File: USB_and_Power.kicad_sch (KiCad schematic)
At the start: 20 parts, among them J1 USB_C_Receptacle_USB2.0_14P, U3 BQ24074RGT, U4 FUSB303BTMX

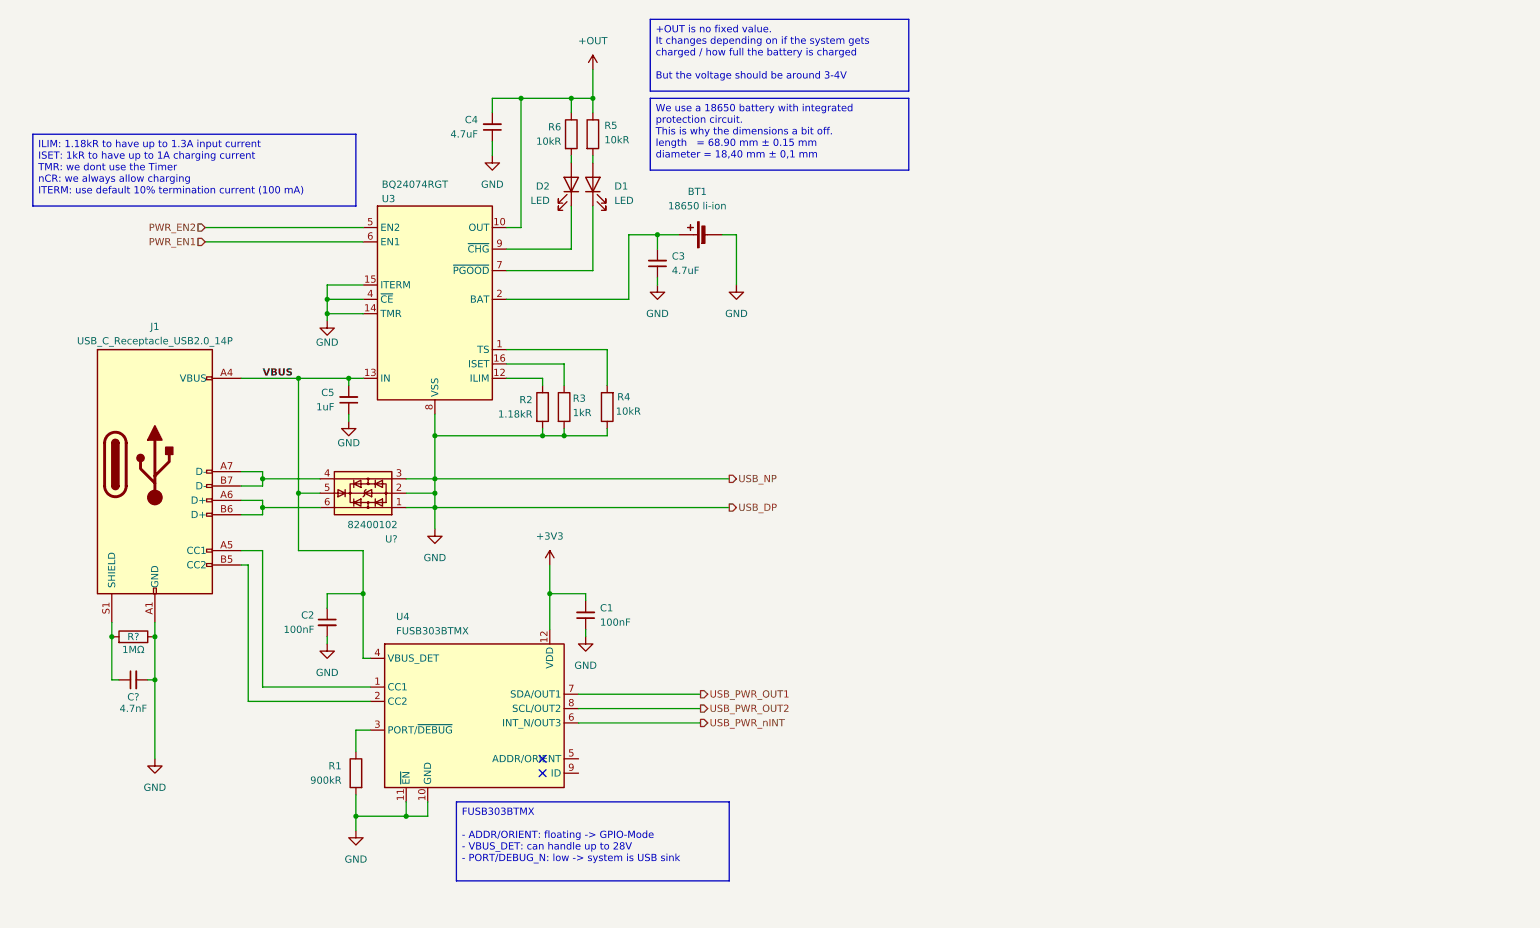
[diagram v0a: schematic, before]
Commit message: Added 5V, 3V3, PAM circuit
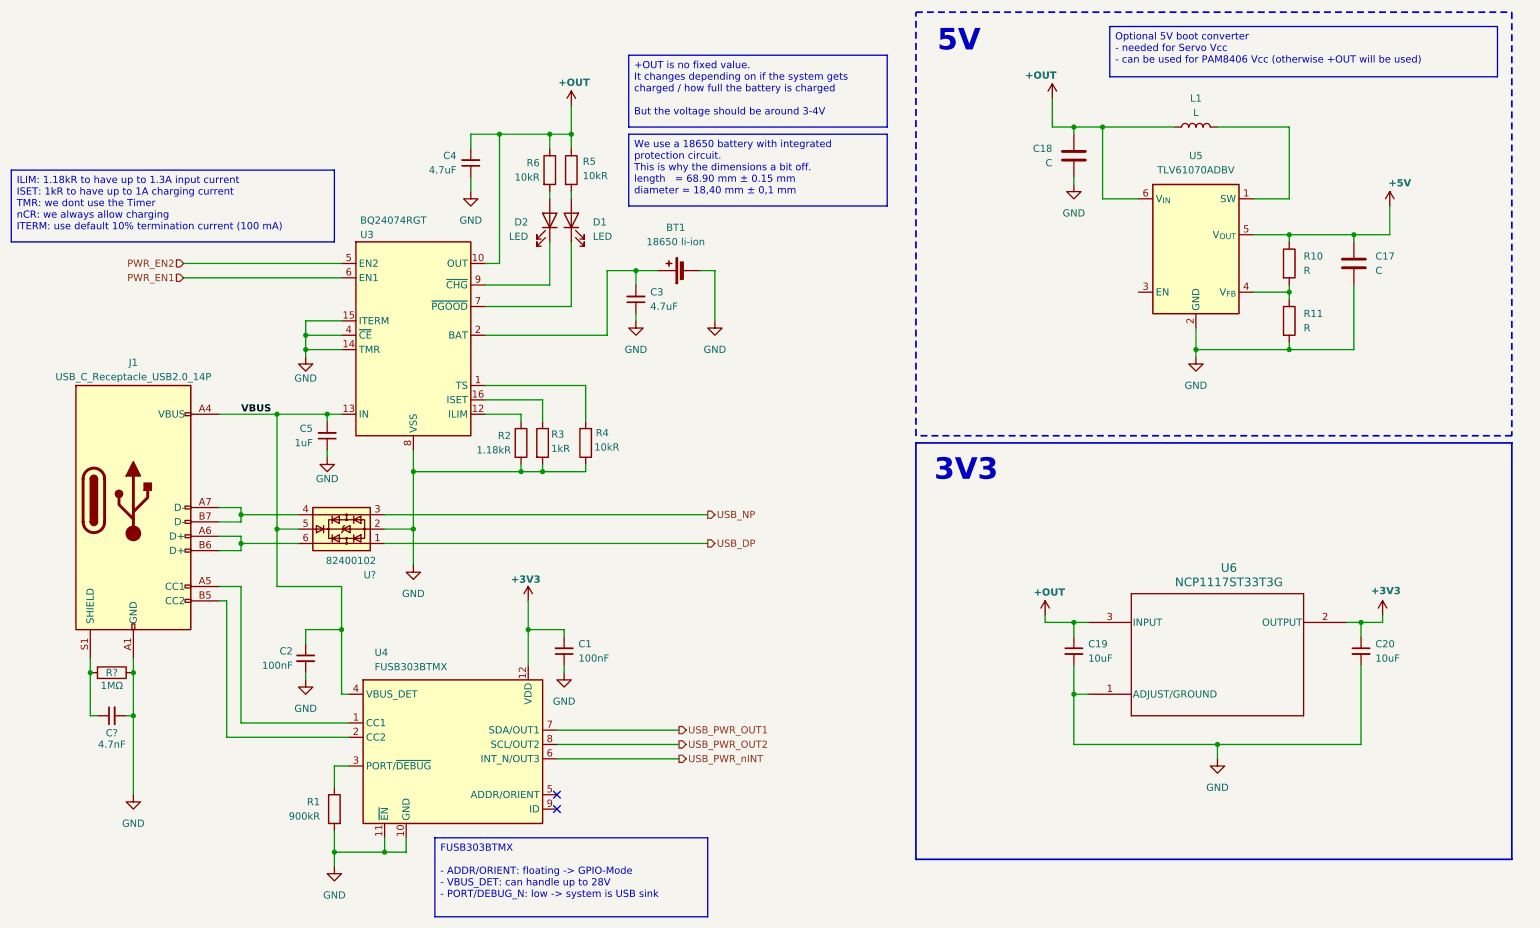
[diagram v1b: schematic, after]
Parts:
- added C17, C18: C, symbol Device:C
- added C19, C20: 10uF, Capacitor_SMD:C_0805_2012Metric_Pad1.18x1.45mm_HandSolder, symbol Device:C_Small
- added L1: L, symbol Device:L
- added R10, R11: R, symbol Device:R
- added U5: TLV61070ADBV, Package_DFN_QFN:Texas_RWU0007A_VQFN-7_2x2mm_P0.5mm, symbol Regulator_Switching:TLV61070ADBV
- added U6: NCP1117ST33T3G, NCP1117ST33T3G:SOT223-3_ONS, symbol NCP1117ST33T3G:NCP1117ST33T3G
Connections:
- net +3V3: now also C20.1, U6.2 (OUTPUT)
- net +OUT: now also C18.1, C19.1, L1.1, U5.6 (V_{IN}), U6.3 (INPUT)
- net GND: now also C17.2, C18.2, C19.2, C20.2, R11.2, U5.2 (GND), U6.1 (ADJUST/GROUND); no longer U?.1, U?.3
- new net: L1.2, U5.1 (SW)
- new net: R10.2, R11.1, U5.4 (V_{FB})
- new net +5V: C17.1, R10.1, U5.5 (V_{OUT})
- new net USB_DP: U?.1
- new net USB_NP: U?.3
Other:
- note added: "3V3"
- note added: "5V"
- company: (none) -> Author: Christian R
- title: (none) -> Snail v1
- moved on the sheet: BT1, C1, C2, C3, C4, C5, C?, D1, D2, J1, R1, R2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

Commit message: Added BY25Q32 extFlash
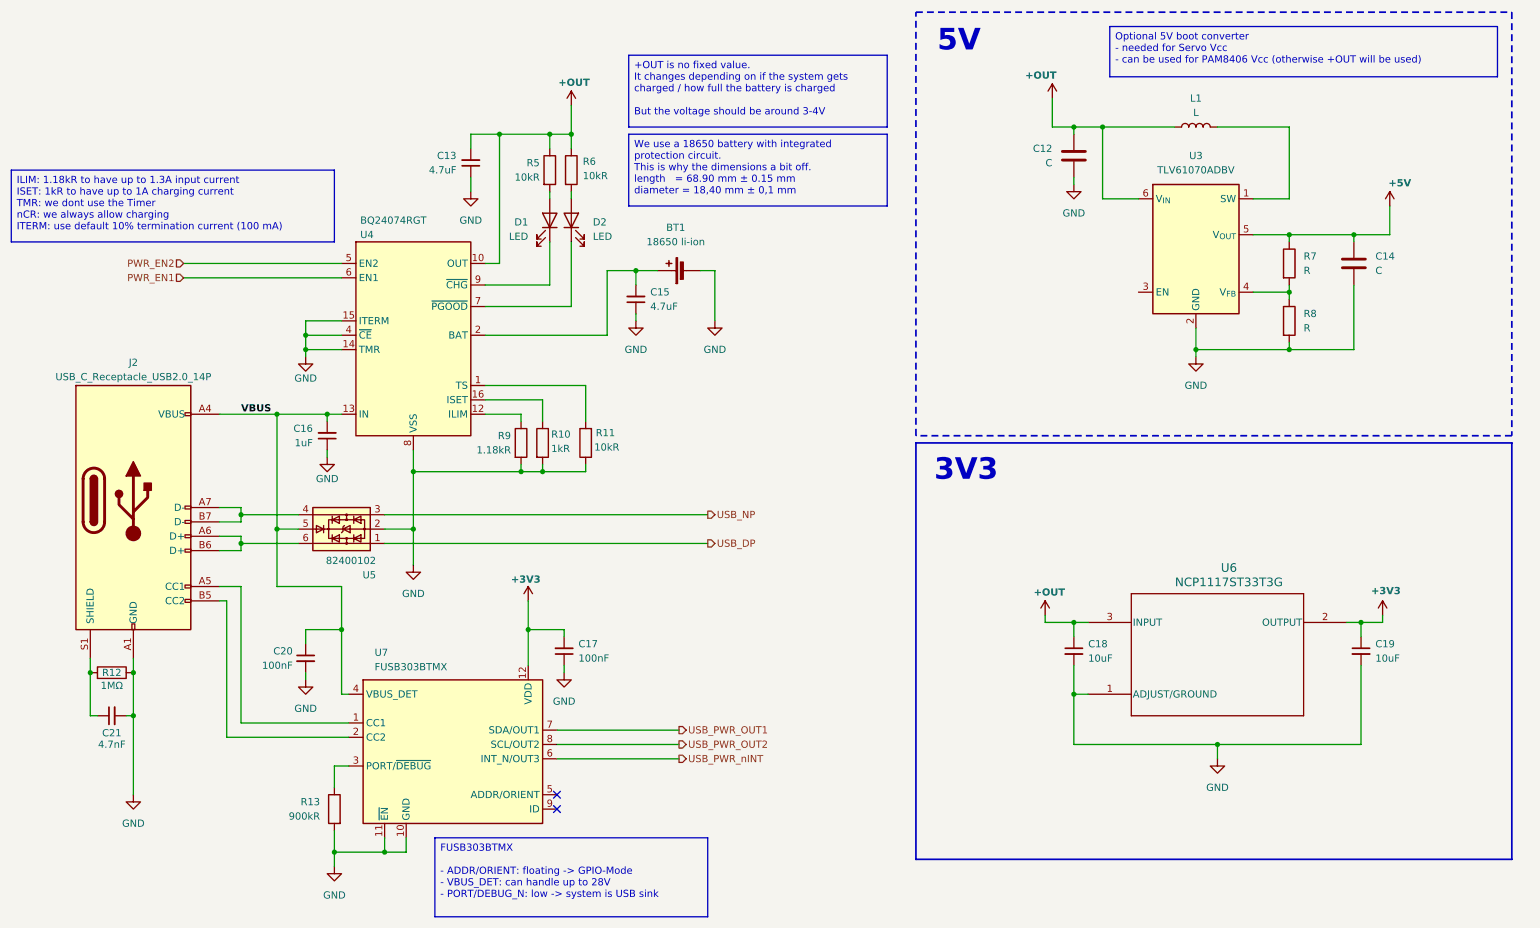
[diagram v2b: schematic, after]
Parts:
- gave numbers to parts that had none: 3
- renumbered C18 to C12, C4 to C13, C17 to C14, C3 to C15, C5 to C16, C1 to C17, C19 to C18, C20 to C19, C2 to C20, D2 to D1, D1 to D2, J1 to J2, R3 to R10, R4 to R11, R1 to R13, R6 to R5, R5 to R6, R10 to R7, R11 to R8, R2 to R9, U5 to U3, U3 to U4, U4 to U7

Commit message: Changed LDO to Buc-Boost
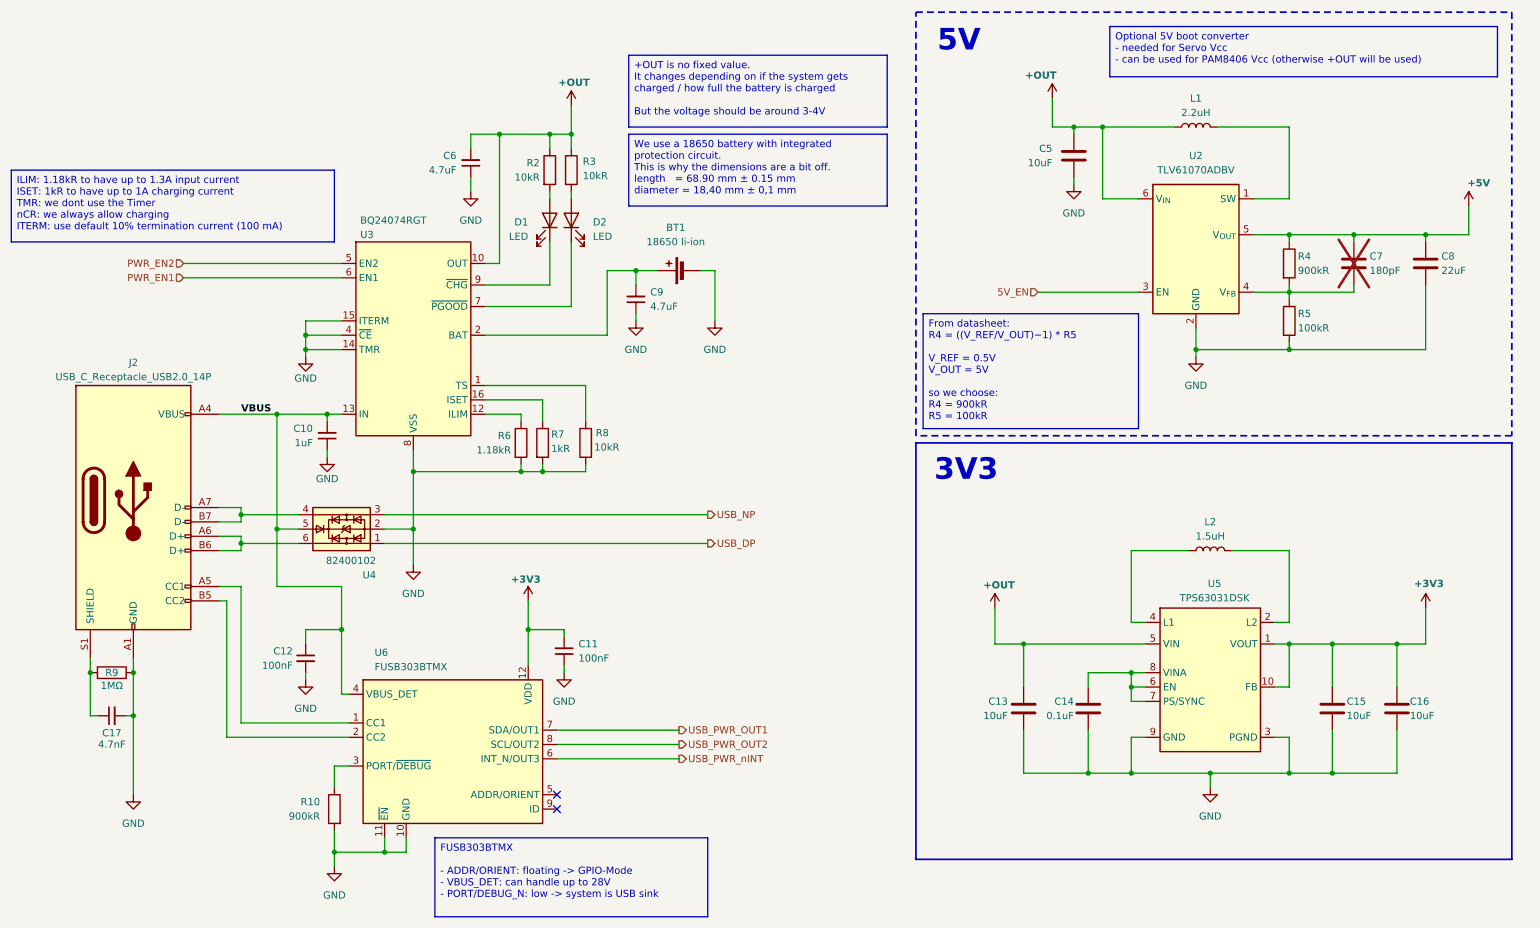
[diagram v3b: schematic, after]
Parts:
- removed C18, C19: 10uF, Capacitor_SMD:C_0805_2012Metric_Pad1.18x1.45mm_HandSolder, symbol Device:C_Small
- removed U6: NCP1117ST33T3G, NCP1117ST33T3G:SOT223-3_ONS, symbol NCP1117ST33T3G:NCP1117ST33T3G
- added C13, C15, C16: 10uF, Capacitor_SMD:C_0805_2012Metric_Pad1.18x1.45mm_HandSolder, symbol Device:C
- added C14: 0.1uF, Capacitor_SMD:C_0805_2012Metric_Pad1.18x1.45mm_HandSolder, symbol Device:C
- added C8: 22uF, Capacitor_SMD:C_0805_2012Metric_Pad1.18x1.45mm_HandSolder, symbol Device:C
- added L2: 1.5uH, Inductor_SMD:L_0805_2012Metric_Pad1.05x1.20mm_HandSolder, symbol Device:L
- added U5: TPS63031DSK, Package_SON:WSON-10-1EP_2.5x2.5mm_P0.5mm_EP1.2x2mm, symbol Regulator_Switching:TPS63031DSK
- C10: renamed from C16; footprint (none) -> Capacitor_SMD:C_0805_2012Metric_Pad1.18x1.45mm_HandSolder
- C11: renamed from C17; footprint (none) -> Capacitor_SMD:C_0805_2012Metric_Pad1.18x1.45mm_HandSolder
- C12: renamed from C20; footprint (none) -> Capacitor_SMD:C_0805_2012Metric_Pad1.18x1.45mm_HandSolder
- C5: renamed from C12; value C -> 10uF; footprint (none) -> Capacitor_SMD:C_0805_2012Metric_Pad1.18x1.45mm_HandSolder
- C6: renamed from C13; footprint (none) -> Capacitor_SMD:C_0805_2012Metric_Pad1.18x1.45mm_HandSolder
- C7: renamed from C14; value C -> 180pF; footprint (none) -> Capacitor_SMD:C_0805_2012Metric_Pad1.18x1.45mm_HandSolder; now not fitted
- C9: renamed from C15; footprint (none) -> Capacitor_SMD:C_0805_2012Metric_Pad1.18x1.45mm_HandSolder
- D1, D2: footprint (none) -> LED_SMD:LED_0805_2012Metric_Pad1.15x1.40mm_HandSolder
- J2: footprint (none) -> Connector_USB:USB_C_Receptacle_GCT_USB4105-xx-A_16P_TopMnt_Horizontal
- L1: value L -> 2.2uH; footprint (none) -> Inductor_SMD:L_0805_2012Metric_Pad1.05x1.20mm_HandSolder
- R10: renamed from R13; footprint (none) -> Resistor_SMD:R_0805_2012Metric_Pad1.20x1.40mm_HandSolder
- R2: renamed from R5; footprint (none) -> Resistor_SMD:R_0805_2012Metric_Pad1.20x1.40mm_HandSolder
- R3: renamed from R6; footprint (none) -> Resistor_SMD:R_0805_2012Metric_Pad1.20x1.40mm_HandSolder
- R4: renamed from R7; value R -> 900kR; footprint (none) -> Resistor_SMD:R_0805_2012Metric_Pad1.20x1.40mm_HandSolder
- R5: renamed from R8; value R -> 100kR; footprint (none) -> Resistor_SMD:R_0805_2012Metric_Pad1.20x1.40mm_HandSolder
- R6: renamed from R9; footprint (none) -> Resistor_SMD:R_0805_2012Metric_Pad1.20x1.40mm_HandSolder
- R7: renamed from R10; footprint (none) -> Resistor_SMD:R_0805_2012Metric_Pad1.20x1.40mm_HandSolder
- R8: renamed from R11; footprint (none) -> Resistor_SMD:R_0805_2012Metric_Pad1.20x1.40mm_HandSolder
- renumbered C21 to C17, R12 to R9, U3 to U2, U4 to U3, U5 to U4, U7 to U6
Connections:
- net +3V3: now also C15.1, C16.1, U5.1 (VOUT), U5.10 (FB)
- net +5V: now also C8.1
- net +OUT: now also C13.1, U5.5 (VIN)
- net GND: now also C13.2, C14.2, C15.2, C16.2, C8.2, U5.3 (PGND), U5.9 (GND); no longer C7.2
- net 5V_EN: now reaches U2.3 (EN)
- net at R4.2, R5.1, U2.4 (V_{FB}): now also C7.2
- new net: L2.2, U5.2 (L2)
- new net: L2.1, U5.4 (L1)
- new net: C14.1, U5.6 (EN), U5.7 (PS/SYNC), U5.8 (VINA)

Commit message: Added LEDs + TPs
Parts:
- BT1: footprint (none) -> Battery:BatteryHolder_MPD_BH-18650-PC
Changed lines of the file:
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@@
 			)
 		)
-		(property "Footprint" ""
+		(property "Footprint" "Battery:BatteryHolder_MPD_BH-18650-PC"
 			(at 135.636 59.69 90)
 			(effects

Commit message: Started with layout
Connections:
- net +OUT: now also D1.2 (A), D2.2 (A); no longer R2.1, R3.1
- net at D2.1 (K): now also R3.1; no longer U3.7 (~{PGOOD})
- net at R3.2: now also U3.7 (~{PGOOD}); no longer D2.2 (A)
- net at U3.9 (~{CHG}): now also R2.2; no longer D1.1 (K)
- net USB_DP renamed USB+
- net USB_NP renamed USB-
- new net: D1.1 (K), R2.1
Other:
- moved on the sheet: D1, D2, R2, R3
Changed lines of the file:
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@@
 		)
 	)
-	(hierarchical_label "USB_NP"
+	(hierarchical_label "USB-"
 		(shape output)
 		(at 140.97 102.87 0)
@@
 		)
 	)
-	(hierarchical_label "USB_DP"
+	(hierarchical_label "USB+"
 		(shape output)
 		(at 140.97 107.95 0)
@@
 	(symbol
 		(lib_id "Device:LED")
-		(at 116.84 50.8 90)
+		(at 116.84 41.91 90)
 		(unit 1)
 		(exclude_from_sim no)
@@
 		(fields_autoplaced yes)
 		(property "Reference" "D2"
-			(at 120.65 51.1174 90)
+			(at 120.65 42.2274 90)
 			(effects
 				(font
@@
 		)
 		(property "Value" "LED"
-			(at 120.65 53.6574 90)
+			(at 120.65 44.7674 90)
 			(effects
 				(font
@@
 		)
 		(property "Footprint" "LED_SMD:LED_0805_2012Metric_Pad1.15x1.40mm_HandSolder"
-			(at 116.84 50.8 0)
+			(at 116.84 41.91 0)
 			(effects
 				(font
@@
 		)
 		(property "Datasheet" "~"
-			(at 116.84 50.8 0)
+			(at 116.84 41.91 0)
 			(effects
 				(font
@@
 		)
 		(property "Description" "Light emitting diode"
-			(at 116.84 50.8 0)
+			(at 116.84 41.91 0)
 			(effects
 				(font
@@
 		)
 		(property "Sim.Pins" "1=K 2=A"
-			(at 116.84 50.8 0)
+			(at 116.84 41.91 0)
 			(effects
 				(font
@@
 	(symbol
 		(lib_id "Device:LED")
-		(at 113.03 50.8 270)
+		(at 113.03 41.91 270)
 		(mirror x)
 		(unit 1)
@@
 		(dnp no)
 		(property "Reference" "D1"
-			(at 109.22 51.1174 90)
+			(at 109.22 42.2274 90)
 			(effects
 				(font
@@
 		)
 		(property "Value" "LED"
-			(at 109.22 53.6574 90)
+			(at 109.22 44.7674 90)
 			(effects
 				(font
@@
 		)
 		(property "Footprint" "LED_SMD:LED_0805_2012Metric_Pad1.15x1.40mm_HandSolder"
-			(at 113.03 50.8 0)
+			(at 113.03 41.91 0)
 			(effects
 				(font
@@
 		)
 		(property "Datasheet" "~"
-			(at 113.03 50.8 0)
+			(at 113.03 41.91 0)
 			(effects
 				(font
@@
 		)
 		(property "Description" "Light emitting diode"
-			(at 113.03 50.8 0)
+			(at 113.03 41.91 0)
 			(effects
 				(font
@@
 		)
 		(property "Sim.Pins" "1=K 2=A"
-			(at 113.03 50.8 0)
+			(at 113.03 41.91 0)
 			(effects
 				(font
@@
 	(symbol
 		(lib_id "Device:R")
-		(at 116.84 41.91 0)
+		(at 116.84 50.8 0)
 		(unit 1)
 		(exclude_from_sim no)
@@
 		(dnp no)
 		(property "Reference" "R3"
-			(at 118.872 40.386 0)
+			(at 118.872 49.276 0)
 			(effects
 				(font
@@
 		)
 		(property "Value" "10kR"
-			(at 118.872 42.926 0)
+			(at 118.872 51.816 0)
 			(effects
 				(font
@@
 		)
 		(property "Footprint" "Resistor_SMD:R_0805_2012Metric_Pad1.20x1.40mm_HandSolder"
-			(at 115.062 41.91 90)
+			(at 115.062 50.8 90)
 			(effects
 				(font
@@
 		)
 		(property "Datasheet" "~"
-			(at 116.84 41.91 0)
+			(at 116.84 50.8 0)
 			(effects
 				(font
@@
 		)
 		(property "Description" "Resistor"
-			(at 116.84 41.91 0)
+			(at 116.84 50.8 0)
 			(effects
 				(font
@@
 	(symbol
 		(lib_id "Device:R")
-		(at 113.03 41.91 0)
+		(at 113.03 50.8 0)
 		(unit 1)
 		(exclude_from_sim no)
@@
 		(dnp no)
 		(property "Reference" "R2"
-			(at 111.252 40.64 0)
+			(at 111.252 49.53 0)
 			(effects
 				(font
@@
 		)
 		(property "Value" "10kR"
-			(at 111.252 43.18 0)
+			(at 111.252 52.07 0)
 			(effects
 				(font
@@
 		)
 		(property "Footprint" "Resistor_SMD:R_0805_2012Metric_Pad1.20x1.40mm_HandSolder"
-			(at 111.252 41.91 90)
+			(at 111.252 50.8 90)
 			(effects
 				(font
@@
 		)
 		(property "Datasheet" "~"
-			(at 113.03 41.91 0)
+			(at 113.03 50.8 0)
 			(effects
 				(font
@@
 		)
 		(property "Description" "Resistor"
-			(at 113.03 41.91 0)
+			(at 113.03 50.8 0)
 			(effects
 				(font
